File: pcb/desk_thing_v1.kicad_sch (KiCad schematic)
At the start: 6 parts, among them SW1 RotaryEncoder_Switch, SW2 SW_Push, SW3 SW_Push, SW4 SW_Push, U1 Pico

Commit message: PCB v1.1
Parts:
- removed SW2, SW3, SW4: SW_Push, Button_Switch_Keyboard:SW_Cherry_MX_1.00u_PCB, symbol Switch:SW_Push
- added SW2, SW3, SW4: SW_Push_LED, desk_thing_lib:SW_Cherry_MX_1.00u_PCB, symbol Switch:SW_Push_LED
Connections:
- net +3V3: now also U1.36 (3V3); no longer U1.37 (3V3_EN)
- net BTN1: now also U1.27 (GPIO21), SW2.2; no longer U1.9 (GPIO6)
- net BTN2: now also U1.25 (GPIO19), SW3.2; no longer U1.10 (GPIO7)
- net BTN3: now also U1.22 (GPIO17), SW4.2; no longer U1.11 (GPIO8)
- net GND: now also SW2.1, SW2.3 (K), SW3.1, SW3.3 (K), SW4.1, SW4.3 (K)
- net ROT_A: now also U1.17 (GPIO13); no longer U1.16 (GPIO12)
- net ROT_B: now also U1.16 (GPIO12); no longer U1.17 (GPIO13)
- net LED3: now reaches U1.21 (GPIO16)
- net LED3: now also SW4.4 (A)
- net LED2: now reaches U1.24 (GPIO18)
- net LED2: now also SW3.4 (A)
- net LED1: now reaches U1.26 (GPIO20)
- net LED1: now also SW2.4 (A)
- no-connect marks 3 -> 20

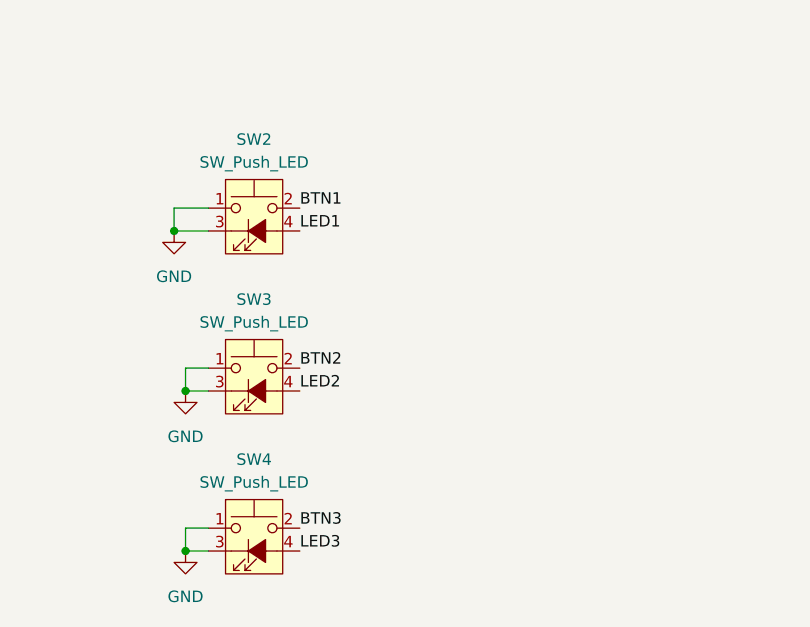
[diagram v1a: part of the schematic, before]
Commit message: Fix PCB mistakes
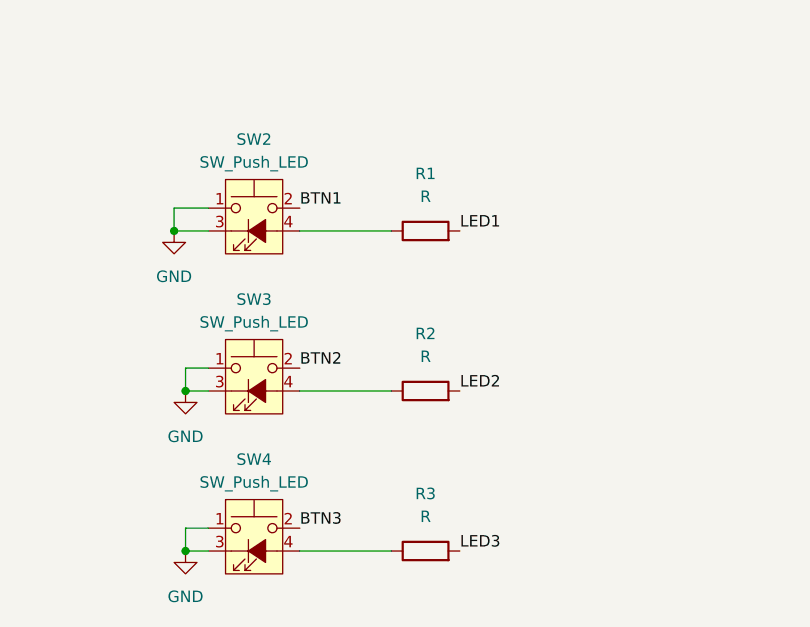
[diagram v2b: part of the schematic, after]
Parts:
- added R1, R2, R3: R, Resistor_SMD:R_1206_3216Metric, symbol Device:R
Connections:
- net LED1: now also R1.2; no longer SW2.4 (A)
- net LED2: now also R2.2; no longer SW3.4 (A)
- net LED3: now also R3.2; no longer SW4.4 (A)
- new net: R3.1, SW4.4 (A)
- new net: R1.1, SW2.4 (A)
- new net: R2.1, SW3.4 (A)
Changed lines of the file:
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@@
+	(wire
+		(pts
+			(xy 88.9 120.65) (xy 99.06 120.65)
+		)
+		(stroke
+			(width 0)
+			(type default)
+		)
+	)
 	(wire
 		(pts
@@
 	(wire
 		(pts
-			(xy 109.22 43.18) (xy 121.92 43.18)
+			(xy 88.9 156.21) (xy 99.06 156.21)
 		)
 		(stroke
@@
 	(wire
 		(pts
-			(xy 74.93 118.11) (xy 78.74 118.11)
+			(xy 109.22 43.18) (xy 121.92 43.18)
 		)
 		(stroke
@@
 	(wire
 		(pts
-			(xy 168.91 68.58) (xy 177.8 68.58)
+			(xy 74.93 118.11) (xy 78.74 118.11)
 		)
 		(stroke
@@
 	(wire
 		(pts
-			(xy 58.42 63.5) (xy 73.66 63.5)
+			(xy 168.91 68.58) (xy 177.8 68.58)
 		)
 		(stroke
@@
 	(wire
 		(pts
-			(xy 166.37 129.54) (xy 177.8 129.54)
+			(xy 58.42 63.5) (xy 73.66 63.5)
 		)
 		(stroke
@@
 	(wire
 		(pts
-			(xy 74.93 120.65) (xy 74.93 118.11)
+			(xy 166.37 129.54) (xy 177.8 129.54)
 		)
 		(stroke
@@
 	(wire
 		(pts
-			(xy 109.22 50.8) (xy 115.57 50.8)
+			(xy 74.93 120.65) (xy 74.93 118.11)
 		)
 		(stroke
@@
 	(wire
 		(pts
-			(xy 60.96 38.1) (xy 73.66 38.1)
+			(xy 109.22 50.8) (xy 115.57 50.8)
 		)
 		(stroke
@@
 	(wire
 		(pts
-			(xy 66.04 50.8) (xy 73.66 50.8)
+			(xy 60.96 38.1) (xy 73.66 38.1)
 		)
 		(stroke
@@
 		)
 	)
+	(wire
+		(pts
+			(xy 66.04 50.8) (xy 73.66 50.8)
+		)
+		(stroke
+			(width 0)
+			(type default)
+		)
+	)
+	(wire
+		(pts
+			(xy 88.9 138.43) (xy 99.06 138.43)
+		)
+		(stroke
+			(width 0)
+			(type default)
+		)
+	)
 	(label "OLED_CS"
 		(at 73.66 48.26 180)
@@
 	)
 	(label "LED2"
-		(at 88.9 138.43 0)
+		(at 106.68 138.43 0)
 		(fields_autoplaced yes)
 		(effects
@@
 	)
 	(label "LED3"
-		(at 88.9 156.21 0)
+		(at 106.68 156.21 0)
 		(fields_autoplaced yes)
 		(effects
@@
 	)
 	(label "LED1"
-		(at 88.9 120.65 0)
+		(at 106.68 120.65 0)
 		(fields_autoplaced yes)
 		(effects
@@
 	)
 	(symbol
+		(lib_id "Device:R")
+		(at 102.87 156.21 90)
+		(unit 1)
+		(exclude_from_sim no)
+		(in_bom yes)
+		(on_board yes)
+		(dnp no)
+		(fields_autoplaced yes)
+		(property "Reference" "R3"
+			(at 102.87 149.86 90)
+			(effects
+				(font
+					(size 1.27 1.27)
+				)
+			)
+		)
+		(property "Value" "R"
+			(at 102.87 152.4 90)
+			(effects
+				(font
+					(size 1.27 1.27)
+				)
+			)
+		)
+		(property "Footprint" "Resistor_SMD:R_1206_3216Metric"
+			(at 102.87 157.988 90)
+			(effects
+				(font
+					(size 1.27 1.27)
+				)
+				(hide yes)
+			)
+		)
+		(property "Datasheet" "~"
+			(at 102.87 156.21 0)
+			(effects
+				(font
+					(size 1.27 1.27)
+				)
+				(hide yes)
+			)
+		)
+		(property "Description" "Resistor"
+			(at 102.87 156.21 0)
+			(effects
+				(font
+					(size 1.27 1.27)
+				)
+				(hide yes)
+			)
+		)
+		(pin "1"
+		)
+		(pin "2"
+		)
+		(instances
+			(project "desk_thing_v1"
+				(path "/9191b4e7-8143-4f5d-9ea3-848b5b9a7eb0"
+					(reference "R3")
+					(unit 1)
+				)
+			)
+		)
+	)
+	(symbol
 		(lib_id "MCU_RaspberryPi_and_Boards:Pico")
 		(at 91.44 57.15 0)
@@
 	)
 	(symbol
+		(lib_id "Device:R")
+		(at 102.87 120.65 90)
+		(unit 1)
+		(exclude_from_sim no)
+		(in_bom yes)
+		(on_board yes)
+		(dnp no)
+		(fields_autoplaced yes)
+		(property "Reference" "R1"
+			(at 102.87 114.3 90)
+			(effects
+				(font
+					(size 1.27 1.27)
+				)
+			)
+		)
+		(property "Value" "R"
+			(at 102.87 116.84 90)
+			(effects
+				(font
+					(size 1.27 1.27)
+				)
+			)
+		)
+		(property "Footprint" "Resistor_SMD:R_1206_3216Metric"
+			(at 102.87 122.428 90)
+			(effects
+				(font
+					(size 1.27 1.27)
+				)
+				(hide yes)
+			)
+		)
+		(property "Datasheet" "~"
+			(at 102.87 120.65 0)
+			(effects
+				(font
+					(size 1.27 1.27)
+				)
+				(hide yes)
+			)
+		)
+		(property "Description" "Resistor"
+			(at 102.87 120.65 0)
+			(effects
+				(font
+					(size 1.27 1.27)
+				)
+				(hide yes)
+			)
+		)
+		(pin "1"
+		)
+		(pin "2"
+		)
+		(instances
+			(project ""
+				(path "/9191b4e7-8143-4f5d-9ea3-848b5b9a7eb0"
+					(reference "R1")
+					(unit 1)
+				)
+			)
+		)
+	)
+	(symbol
 		(lib_id "power:GND")
 		(at 166.37 130.81 0)
@@
 					(unit 1)
 				)
+			)
+		)
+	)
+	(symbol
+		(lib_id "Device:R")
+		(at 102.87 138.43 90)
+		(unit 1)
+		(exclude_from_sim no)
+		(in_bom yes)
+		(on_board yes)
+		(dnp no)
+		(fields_autoplaced yes)
+		(property "Reference" "R2"
+			(at 102.87 132.08 90)
+			(effects
+				(font
+					(size 1.27 1.27)
+				)
+			)
+		)
+		(property "Value" "R"
+			(at 102.87 134.62 90)
+			(effects
+				(font
+					(size 1.27 1.27)
+				)
+			)
+		)
+		(property "Footprint" "Resistor_SMD:R_1206_3216Metric"
+			(at 102.87 140.208 90)
+			(effects
+				(font
+					(size 1.27 1.27)
+				)
+				(hide yes)
+			)
+		)
+		(property "Datasheet" "~"
+			(at 102.87 138.43 0)
+			(effects
+				(font
+					(size 1.27 1.27)
+				)
+				(hide yes)
+			)
+		)
+		(property "Description" "Resistor"
+			(at 102.87 138.43 0)
+			(effects
+				(font
+					(size 1.27 1.27)
+				)
+				(hide yes)
+			)
+		)
+		(pin "1"
+		)
+		(pin "2"
+		)
+		(instances
+			(project "desk_thing_v1"
+				(path "/9191b4e7-8143-4f5d-9ea3-848b5b9a7eb0"
+					(reference "R2")
+					(unit 1)
+				)
